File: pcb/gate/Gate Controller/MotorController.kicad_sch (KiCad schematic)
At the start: 25 parts, among them IC1 MCP23009-E_SS, J1 CN7, J10 Conn_01x08_Female, J11 Left Post, J12 Conn_01x08_Female, J2 Conn_01x04_Female, J3 CN7, J4 CN1, J5 Conn_01x04_Female, J6 Safety Stop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

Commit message: latest updates
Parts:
- removed J10, J12: Conn_01x08_Female, symbol Connector:Conn_01x08_Female
- removed J11: Left Post, Connector_JST:JST_XH_PinSWAP, symbol Connector:Conn_01x08_Male
- removed J9: Raspberry Controller, Connector_JST:JST_XH_PinSWAP, symbol Connector:Conn_01x08_Male
- added J10, J9: RJ45_Shielded, Connector_RJ:RJ45_Amphenol_RJHSE5380, symbol Connector:RJ45_Shielded
- added SW4: SW_Push, Button_Switch_THT:TS-D015, symbol Switch:SW_Push
- added U1: ~, Logos:QRCode Github Automation, symbol Graphic:QR_Automation
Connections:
- net 3V3: now also J9.8
- net ANTENNA+: now also J10.8
- net CN1_(FL)-: now also J10.4
- net CN1_24v(FL): now also J10.3, J9.3
- net GND: now also J10.5, J10.SH, J9.6, J9.SH, SW4.2
- net PH1: now also J10.7
- net REED LEFT: now also J9.7
- net SCL1: now also J9.4
- net SDA1: now also J9.5
- net START: now also J10.6, SW4.1
- new net +12v: J10.1, J9.1
- new net GATE_LED_COM: J10.2, J9.2

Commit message: reworked to add i2c pullups and reduces unusedd components
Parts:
- removed J5: Conn_01x04_Female, symbol Connector:Conn_01x02_Female
- removed J6: Safety Stop, Connector_JST:JST_EH_S2B-EH_1x02_P2.50mm_Horizontal, symbol Connector:Conn_01x02_Male
- removed J7: Conn_01x02_Female, symbol Connector:Conn_01x02_Female
- removed J8: Detect Gate Open, Connector_JST:JST_EH_S2B-EH_1x02_P2.50mm_Horizontal, symbol Connector:Conn_01x02_Male
- removed SW1: Safety Stop SW, symbol Switch:SW_Push
- removed SW2: SW_Reed, symbol Switch:SW_Reed
- added C1: 0.1uF, Capacitor_SMD:C_1206_3216Metric, symbol Device:C
- renumbered J9 to J5, J10 to J6, SW4 to SW1
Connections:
- net REED LEFT is gone; now on net GND: J5.7
- net 3V3: now also J5.6, C1.1; no longer J5.8
- net GND: now also J5.5, C1.2; no longer J5.6
- net SDA1: now also J5.8; no longer J5.5

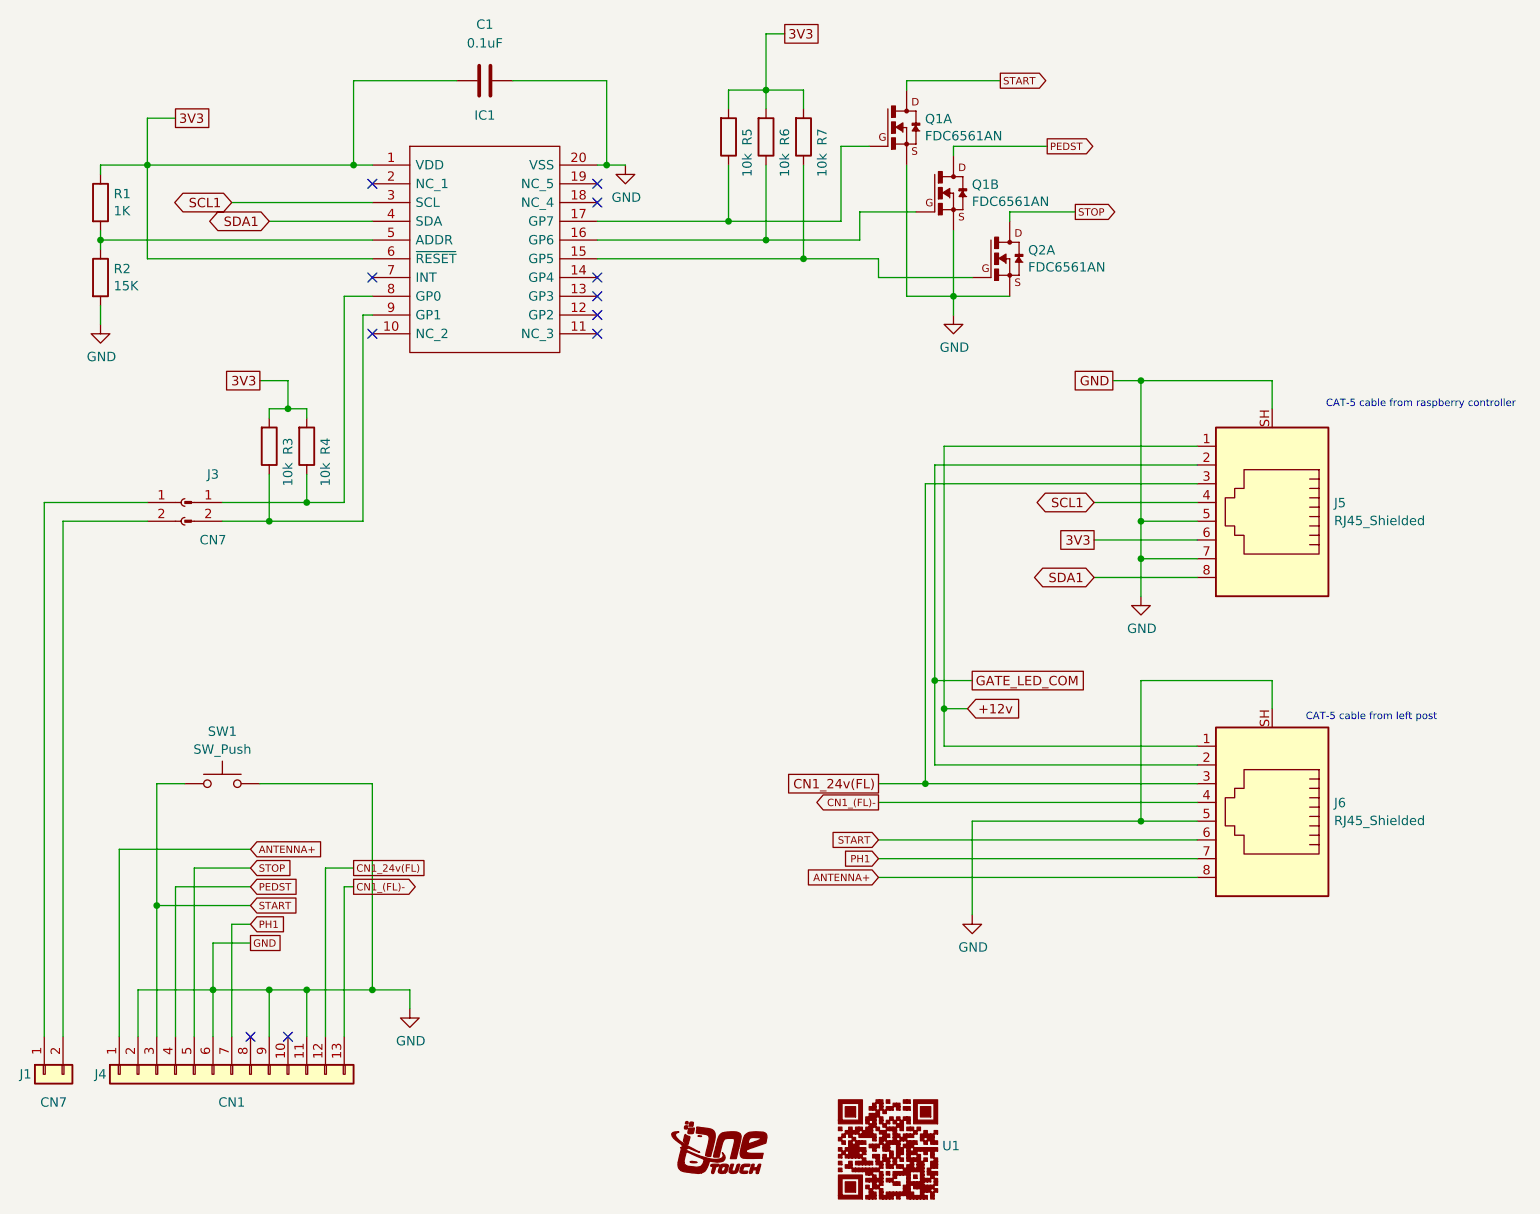
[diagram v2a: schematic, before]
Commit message: Update with latest changes to fix comms issues
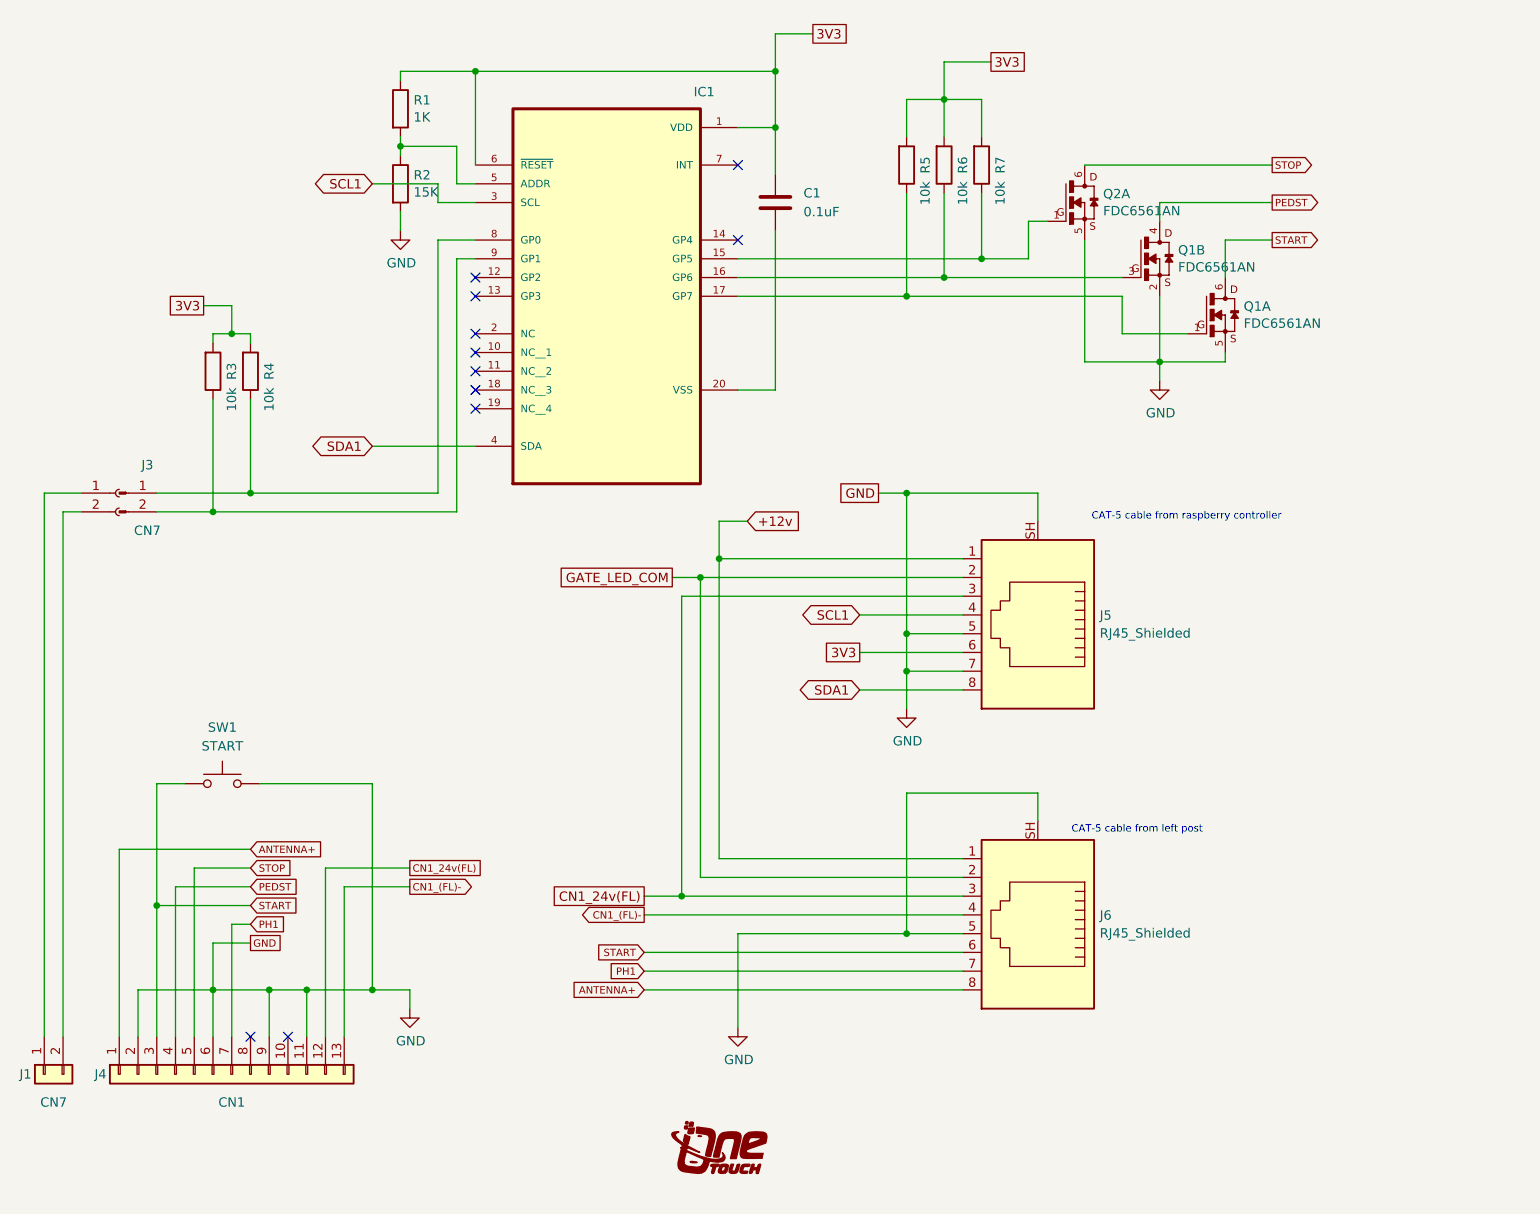
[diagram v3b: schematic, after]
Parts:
- removed U1: ~, Logos:QRCode Github Automation, symbol Graphic:QR_Automation
- IC1: footprint MCP23009-E_SS:SOP65P780X200-20N -> MCP23009_E_SS:SOP65P780X200-20N; MANUFACTURER (none) -> Microchip; MAXIMUM_PACKAGE_HEIGHT (none) -> 2 mm; PARTREV (none) -> C; STANDARD (none) -> IPC 7351B
- SW1: value SW_Push -> START
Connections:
- net 3V3: now also C1.2; no longer C1.1
- net GND: no longer C1.2, IC1.20 (VSS)
- new net: C1.1, IC1.20 (VSS)
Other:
- moved on the sheet: C1, J3, J5, J6, R1, R2, R3, R4, R5, R6, R7
